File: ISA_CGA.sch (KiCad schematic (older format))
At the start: 17 parts, among them U1 74S112, U11 74LS74, U12 74LS393, U13 74LS08, U14 74LS32, U15 74LS00, U28 74LS10, U29 74S04, U3 74S86, U30 74LS32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

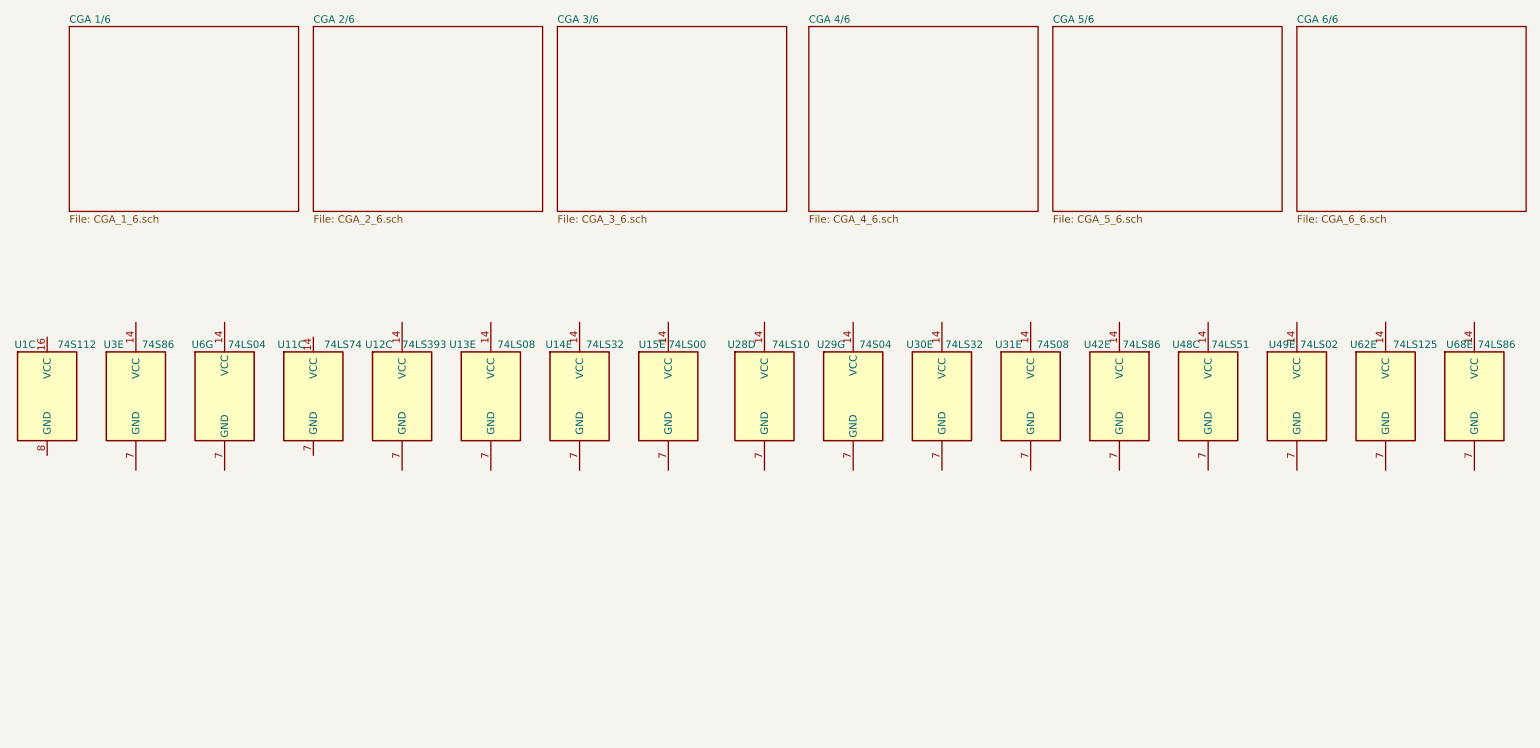
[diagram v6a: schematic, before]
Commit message: More power inputs
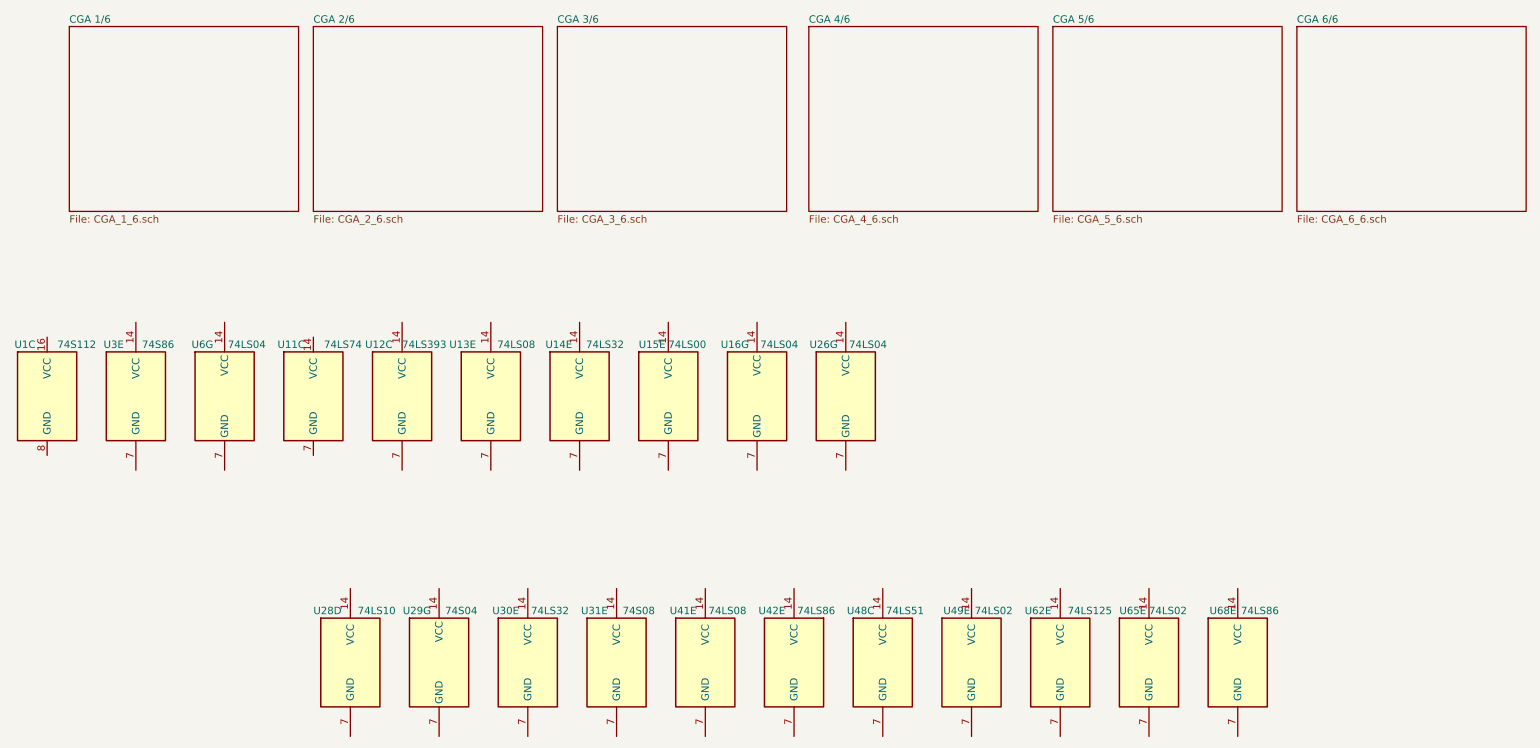
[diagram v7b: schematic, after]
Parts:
- added U16, U26: 74LS04, Package_DIP:DIP-14_W7.62mm_LongPads, symbol 74xx:74LS04
- added U41: 74LS08, Package_DIP:DIP-14_W7.62mm_LongPads, symbol 74xx:74LS08
- added U65: 74LS02, Package_DIP:DIP-14_W7.62mm_LongPads, symbol 74xx:74LS02
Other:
- moved on the sheet: U28D, U29G, U30E, U31E, U42E, U48C, U49E, U62E, U68E
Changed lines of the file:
@@
 L 74xx:74LS51 U?
 U 3 1 604901DC
-P 8750 3350
+P 6550 5150
 AR Path="/60463BAE/604901DC" Ref="U?"  Part="1"
 AR Path="/604901DC" Ref="U48"  Part="3"
-F 0 "U48" H 8600 3700 50  0000 C CNN
-F 1 "74LS51" H 8900 3700 50  0000 C CNN
-F 2 "Package_DIP:DIP-14_W7.62mm_LongPads" H 8750 3350 50  0001 C CNN
-F 3 "http://www.ti.com/lit/ds/symlink/sn74ls51.pdf" H 8750 3350 50  0001 C CNN
-	3    8750 3350
+F 0 "U48" H 6400 5500 50  0000 C CNN
+F 1 "74LS51" H 6700 5500 50  0000 C CNN
+F 2 "Package_DIP:DIP-14_W7.62mm_LongPads" H 6550 5150 50  0001 C CNN
+F 3 "http://www.ti.com/lit/ds/symlink/sn74ls51.pdf" H 6550 5150 50  0001 C CNN
+	3    6550 5150
 	1    0    0    -1
 $EndComp
@@
 L 74xx:74LS02 U?
 U 5 1 60495092
-P 9350 3350
+P 7150 5150
 AR Path="/60463BAE/60495092" Ref="U?"  Part="3"
 AR Path="/60495092" Ref="U49"  Part="5"
-F 0 "U49" H 9250 3700 50  0000 C CNN
-F 1 "74LS02" H 9500 3700 50  0000 C CNN
-F 2 "" H 9350 3350 50  0001 C CNN
-F 3 "http://www.ti.com/lit/gpn/sn74ls02" H 9350 3350 50  0001 C CNN
-	5    9350 3350
+F 0 "U49" H 7050 5500 50  0000 C CNN
+F 1 "74LS02" H 7300 5500 50  0000 C CNN
+F 2 "" H 7150 5150 50  0001 C CNN
+F 3 "http://www.ti.com/lit/gpn/sn74ls02" H 7150 5150 50  0001 C CNN
+	5    7150 5150
 	1    0    0    -1
 $EndComp
@@
 L 74xx:74LS125 U?
 U 5 1 6049EC67
-P 9950 3350
+P 7750 5150
 AR Path="/60463BAE/6049EC67" Ref="U?"  Part="1"
 AR Path="/6049EC67" Ref="U62"  Part="5"
-F 0 "U62" H 9800 3700 50  0000 C CNN
-F 1 "74LS125" H 10150 3700 50  0000 C CNN
-F 2 "Package_DIP:DIP-14_W10.16mm_LongPads" H 9950 3350 50  0001 C CNN
-F 3 "http://www.ti.com/lit/gpn/sn74LS125" H 9950 3350 50  0001 C CNN
-	5    9950 3350
+F 0 "U62" H 7600 5500 50  0000 C CNN
+F 1 "74LS125" H 7950 5500 50  0000 C CNN
+F 2 "Package_DIP:DIP-14_W10.16mm_LongPads" H 7750 5150 50  0001 C CNN
+F 3 "http://www.ti.com/lit/gpn/sn74LS125" H 7750 5150 50  0001 C CNN
+	5    7750 5150
 	1    0    0    -1
 $EndComp
@@
 L 74xx:74LS10 U?
 U 4 1 6073B547
-P 5750 3350
+P 2950 5150
 AR Path="/60463BAE/6073B547" Ref="U?"  Part="3"
 AR Path="/6073B547" Ref="U28"  Part="4"
-F 0 "U28" H 5500 3700 50  0000 L CNN
-F 1 "74LS10" H 5800 3700 50  0000 L CNN
-F 2 "Package_DIP:DIP-14_W7.62mm_LongPads" H 5750 3350 50  0001 C CNN
-F 3 "http://www.ti.com/lit/gpn/sn74LS10" H 5750 3350 50  0001 C CNN
-	4    5750 3350
+F 0 "U28" H 2700 5500 50  0000 L CNN
+F 1 "74LS10" H 3000 5500 50  0000 L CNN
+F 2 "Package_DIP:DIP-14_W7.62mm_LongPads" H 2950 5150 50  0001 C CNN
+F 3 "http://www.ti.com/lit/gpn/sn74LS10" H 2950 5150 50  0001 C CNN
+	4    2950 5150
 	1    0    0    -1
 $EndComp
@@
 L 74xx:74LS86 U?
 U 5 1 61CD3D2F
-P 10550 3350
+P 8950 5150
 AR Path="/60463C10/61CD3D2F" Ref="U?"  Part="4"
 AR Path="/61CD3D2F" Ref="U68"  Part="5"
-F 0 "U68" H 10450 3700 50  0000 C CNN
-F 1 "74LS86" H 10700 3700 50  0000 C CNN
-F 2 "Package_DIP:DIP-14_W7.62mm_LongPads" H 10550 3350 50  0001 C CNN
-F 3 "74xx/74ls86.pdf" H 10550 3350 50  0001 C CNN
-	5    10550 3350
+F 0 "U68" H 8850 5500 50  0000 C CNN
+F 1 "74LS86" H 9100 5500 50  0000 C CNN
+F 2 "Package_DIP:DIP-14_W7.62mm_LongPads" H 8950 5150 50  0001 C CNN
+F 3 "74xx/74ls86.pdf" H 8950 5150 50  0001 C CNN
+	5    8950 5150
 	1    0    0    -1
 $EndComp
@@
 L 74xx:74LS08 U?
 U 5 1 61D13A76
-P 7550 3350
+P 4750 5150
 AR Path="/60463C10/61D13A76" Ref="U?"  Part="3"
 AR Path="/61D13A76" Ref="U31"  Part="5"
-F 0 "U31" H 7400 3700 50  0000 C CNN
-F 1 "74S08" H 7700 3700 50  0000 C CNN
-F 2 "Package_DIP:DIP-14_W7.62mm_LongPads" H 7550 3350 50  0001 C CNN
-F 3 "http://www.ti.com/lit/gpn/sn74LS08" H 7550 3350 50  0001 C CNN
-	5    7550 3350
+F 0 "U31" H 4600 5500 50  0000 C CNN
+F 1 "74S08" H 4900 5500 50  0000 C CNN
+F 2 "Package_DIP:DIP-14_W7.62mm_LongPads" H 4750 5150 50  0001 C CNN
+F 3 "http://www.ti.com/lit/gpn/sn74LS08" H 4750 5150 50  0001 C CNN
+	5    4750 5150
 	1    0    0    -1
 $EndComp
@@
 L 74xx:74LS86 U?
 U 5 1 629C2DFD
-P 8150 3350
+P 5950 5150
 AR Path="/60463C10/629C2DFD" Ref="U?"  Part="4"
 AR Path="/60463C57/629C2DFD" Ref="U?"  Part="1"
 AR Path="/629C2DFD" Ref="U42"  Part="5"
-F 0 "U42" H 8300 3700 50  0000 C CNN
-F 1 "74LS86" H 8000 3700 50  0000 C CNN
-F 2 "Package_DIP:DIP-14_W7.62mm_LongPads" H 8150 3350 50  0001 C CNN
-F 3 "74xx/74ls86.pdf" H 8150 3350 50  0001 C CNN
-	5    8150 3350
+F 0 "U42" H 6100 5500 50  0000 C CNN
+F 1 "74LS86" H 5800 5500 50  0000 C CNN
+F 2 "Package_DIP:DIP-14_W7.62mm_LongPads" H 5950 5150 50  0001 C CNN
+F 3 "74xx/74ls86.pdf" H 5950 5150 50  0001 C CNN
+	5    5950 5150
 	-1   0    0    -1
 $EndComp
@@
 L 74xx:74LS04 U?
 U 7 1 62A8BC3C
-P 6350 3350
+P 3550 5150
 AR Path="/60463C57/62A8BC3C" Ref="U?"  Part="6"
 AR Path="/62A8BC3C" Ref="U29"  Part="7"
-F 0 "U29" H 6200 3700 50  0000 C CNN
-F 1 "74S04" H 6500 3700 50  0000 C CNN
-F 2 "Package_DIP:DIP-14_W7.62mm_LongPads" H 6350 3350 50  0001 C CNN
-F 3 "http://www.ti.com/lit/gpn/sn74LS04" H 6350 3350 50  0001 C CNN
-	7    6350 3350
+F 0 "U29" H 3400 5500 50  0000 C CNN
+F 1 "74S04" H 3700 5500 50  0000 C CNN
+F 2 "Package_DIP:DIP-14_W7.62mm_LongPads" H 3550 5150 50  0001 C CNN
+F 3 "http://www.ti.com/lit/gpn/sn74LS04" H 3550 5150 50  0001 C CNN
+	7    3550 5150
 	1    0    0    -1
 $EndComp
@@
 L 74xx:74LS32 U?
 U 5 1 62AC6F3C
-P 6950 3350
+P 4150 5150
 AR Path="/60463C57/62AC6F3C" Ref="U?"  Part="3"
 AR Path="/62AC6F3C" Ref="U30"  Part="5"
-F 0 "U30" H 6800 3700 50  0000 C CNN
-F 1 "74LS32" H 7100 3700 50  0000 C CNN
-F 2 "" H 6950 3350 50  0001 C CNN
-F 3 "http://www.ti.com/lit/gpn/sn74LS32" H 6950 3350 50  0001 C CNN
-	5    6950 3350
+F 0 "U30" H 4000 5500 50  0000 C CNN
+F 1 "74LS32" H 4300 5500 50  0000 C CNN
+F 2 "" H 4150 5150 50  0001 C CNN
+F 3 "http://www.ti.com/lit/gpn/sn74LS32" H 4150 5150 50  0001 C CNN
+	5    4150 5150
 	1    0    0    -1
 $EndComp
@@
 	1    0    0    -1
 $EndComp
+$Comp
+L 74xx:74LS04 U?
+U 7 1 62C23B1E
+P 5700 3350
+AR Path="/60463C57/62C23B1E" Ref="U?"  Part="1"
+AR Path="/62C23B1E" Ref="U16"  Part="7"
+F 0 "U16" H 5550 3700 50  0000 C CNN
+F 1 "74LS04" H 5850 3700 50  0000 C CNN
+F 2 "Package_DIP:DIP-14_W7.62mm_LongPads" H 5700 3350 50  0001 C CNN
+F 3 "http://www.ti.com/lit/gpn/sn74LS04" H 5700 3350 50  0001 C CNN
+	7    5700 3350
+	1    0    0    -1
+$EndComp
+$Comp
+L 74xx:74LS02 U?
+U 5 1 62C4F9F3
+P 8350 5150
+AR Path="/60463C57/62C4F9F3" Ref="U?"  Part="1"
+AR Path="/62C4F9F3" Ref="U65"  Part="5"
+F 0 "U65" H 8150 5500 50  0000 L CNN
+F 1 "74LS02" H 8350 5500 50  0000 L CNN
+F 2 "Package_DIP:DIP-14_W7.62mm_LongPads" H 8350 5150 50  0001 C CNN
+F 3 "http://www.ti.com/lit/gpn/sn74ls02" H 8350 5150 50  0001 C CNN
+	5    8350 5150
+	1    0    0    -1
+$EndComp
+$Comp
+L 74xx:74LS08 U?
+U 5 1 62CA5B30
+P 5350 5150
+AR Path="/60463C57/62CA5B30" Ref="U?"  Part="4"
+AR Path="/62CA5B30" Ref="U41"  Part="5"
+F 0 "U41" H 5200 5500 50  0000 C CNN
+F 1 "74LS08" H 5500 5500 50  0000 C CNN
+F 2 "Package_DIP:DIP-14_W7.62mm_LongPads" H 5350 5150 50  0001 C CNN
+F 3 "http://www.ti.com/lit/gpn/sn74LS08" H 5350 5150 50  0001 C CNN
+	5    5350 5150
+	1    0    0    -1
+$EndComp
+$Comp
+L 74xx:74LS04 U?
+U 7 1 62CEF608
+P 6300 3350
+AR Path="/60463C57/62CEF608" Ref="U?"  Part="2"
+AR Path="/62CEF608" Ref="U26"  Part="7"
+F 0 "U26" H 6150 3700 50  0000 C CNN
+F 1 "74LS04" H 6450 3700 50  0000 C CNN
+F 2 "Package_DIP:DIP-14_W7.62mm_LongPads" H 6300 3350 50  0001 C CNN
+F 3 "http://www.ti.com/lit/gpn/sn74LS04" H 6300 3350 50  0001 C CNN
+	7    6300 3350
+	1    0    0    -1
+$EndComp

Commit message: More sheet 4
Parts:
- added U2: 74LS74, Package_DIP:DIP-14_W7.62mm_LongPads, symbol 74xx:74LS74
- added U20: 74LS04, Package_DIP:DIP-14_W7.62mm_LongPads, symbol 74xx:74LS04
- added U22, U27, U47: 74LS51, Package_DIP:DIP-14_W7.62mm_LongPads, symbol 74xx:74LS51
- added U23: 74LS32, Package_DIP:DIP-14_W7.62mm_LongPads, symbol 74xx:74LS32
- added U25, U46: 74LS00, Package_DIP:DIP-14_W7.62mm_LongPads, symbol 74xx:74LS00
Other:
- moved on the sheet: U11C, U12C, U13E, U14E, U15E, U16G, U26G, U28D, U30E, U31E, U3E, U41E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
